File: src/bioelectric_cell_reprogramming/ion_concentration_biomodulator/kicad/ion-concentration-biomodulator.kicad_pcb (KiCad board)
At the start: 4 copper layers, 87.5 x 87.5 mm, 53 parts, among them J1 532610671, J10 39-53-2045, J11 Conn_01x14_Pin, J12 Conn_01x14_Pin, J13 39-53-2045, J14 39-53-2045, J15 Conn_ARM_SWD_TagConnect_TC2030, J16 IPL1-104-01-L-D-K, J17 Conn_01x02_Pin, J18 EJ508A, J19 USB_C_Receptacle_USB2.0_14P, J2 532610671, J3 532610671, J4 532610671, J5 S4B-PH-SM4-TB, J6 Conn_01x02_Pin, J7 6620XX11122_66200211122, J8 39-53-2045, J9 IPL1-102-01-L-S-K, Q1 NDT3055L, Q2 NDT3055L, Q3 NDT3055L, Q4 NDT3055L, Q5 NDT3055L, Q6 NDT3055L, SW1 SW_Push, U1 STM32F410CBTx, U2 LM1084-5.0, U3 LM1084-3.3, U4 USBLC6-2SC6

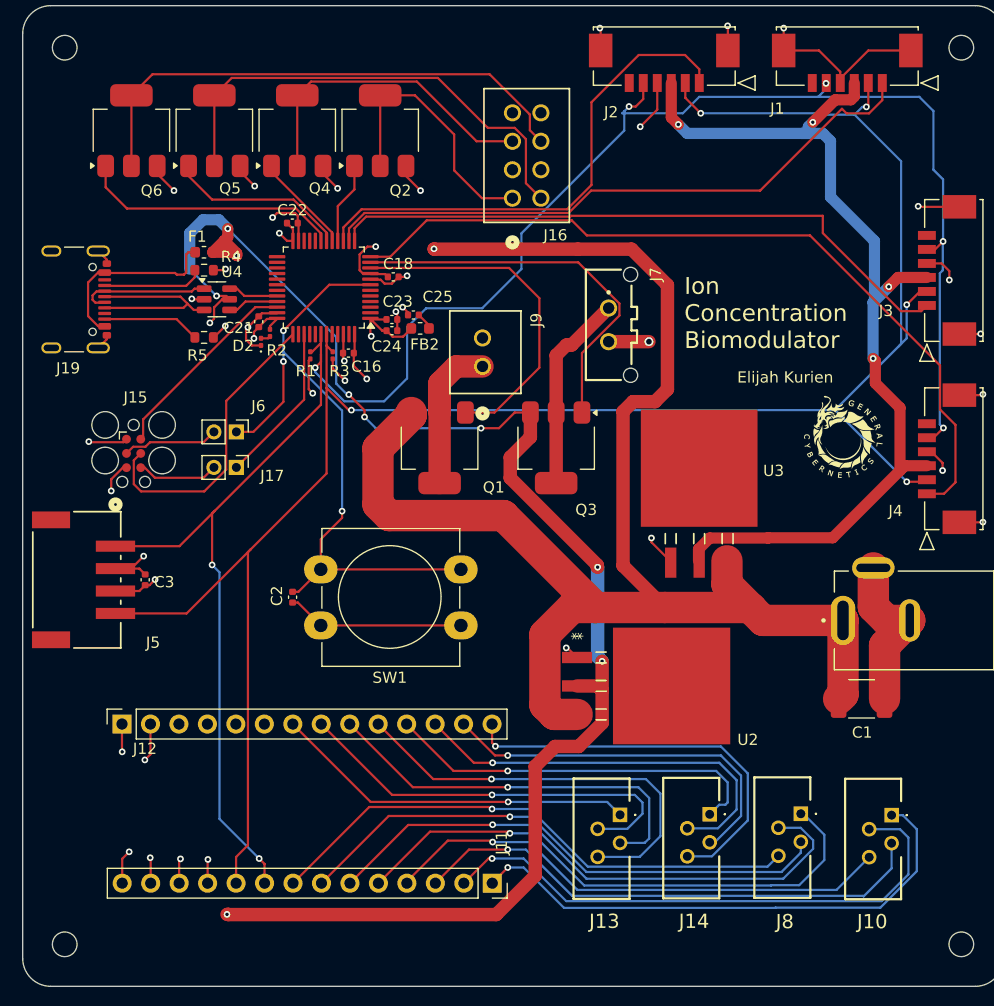
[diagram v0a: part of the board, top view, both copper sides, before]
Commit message: fix: replaced the USB connector with one in the JLCPCB parts library
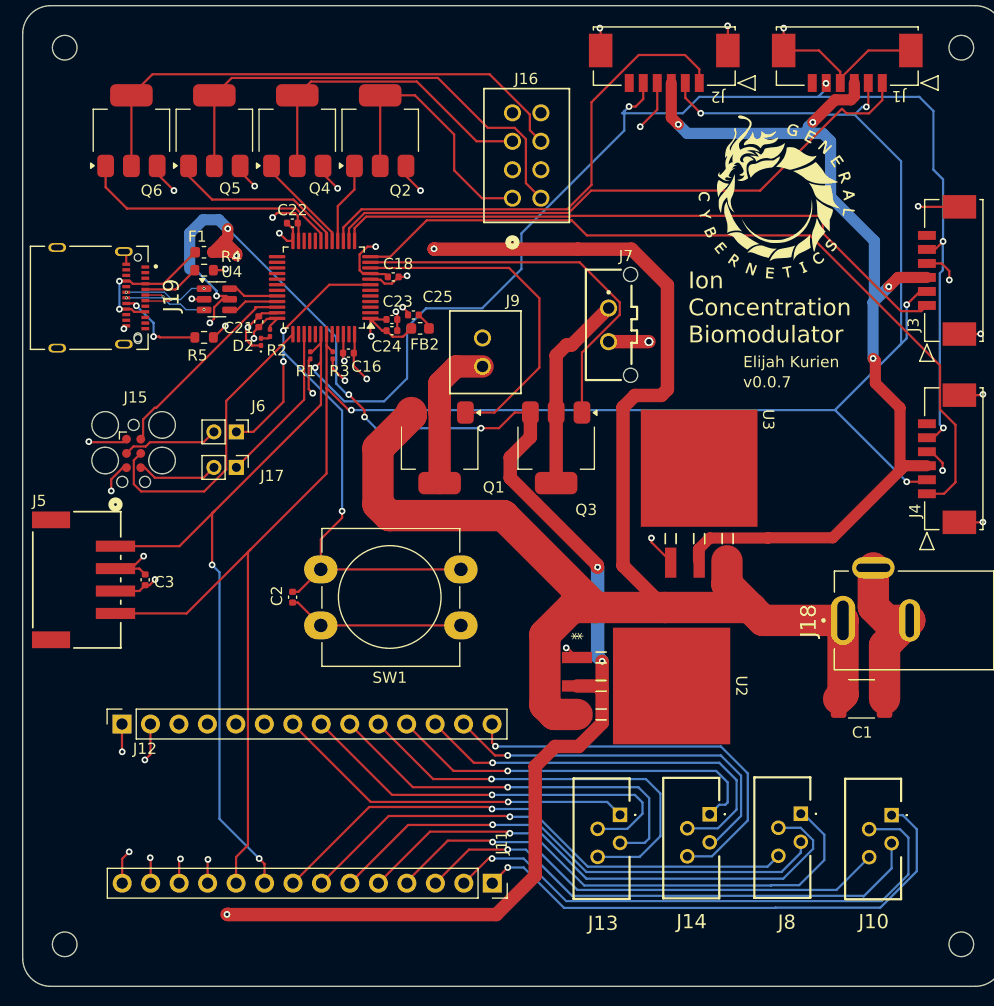
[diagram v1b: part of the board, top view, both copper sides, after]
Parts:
- J1, J2, J3, J4: footprint co2_sensor_footprint:CON_532610671 -> keyed_6_pin_horizontal_0532610671.pretty:CON_532610671
- J10, J13, J14, J8: footprint microfluidics:39532045 -> upright_4_pin_socket_39-53-2045.pretty:39532045
- J16: footprint pinch_solenoid:CONN_IPL1-104-01-x-D-x_SAI -> 2x04_socket_IPL1-104-01-L-D-K.pretty:CONN_IPL1-104-01-x-D-x_SAI
- J18: footprint barrel_jack_EJ508A:MPD_EJ508A -> Barrel_Jack_EJ508A.pretty:MPD_EJ508A
- J19: footprint Connector_USB:USB_C_Receptacle_GCT_USB4105-xx-A_16P_TopMnt_Horizontal -> 12401610E4_2A.pretty:AMPHENOL_12401610E4_2A
- J5: footprint co2_dev_board_male_socket:CONN4_S4B-PH-SM4-TB_JST -> male_socket_S4B-PH-SM4-TB.pretty:CONN4_S4B-PH-SM4-TB_JST
- J7: footprint peltier_cooler_socket_footprint:66200211122 -> 1x02_socket_66200211122.pretty:66200211122
- J9: footprint solenoid_footprint:CONN_IPL1-102-01-L-S-K_SAI -> 1x02_socket_IPL1-102-01-L-S-K.pretty:CONN_IPL1-102-01-L-S-K_SAI
- U2, U3: footprint LDO_5V:TS3B -> LDO_5V_LM1084.pretty:TS3B
- moved G*** 22.5 mm to (167.8, 66.3)
- moved J19 6.65 mm to (110.8, 75.3)
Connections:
- J19 pad A6: /D+ -> /D+_in
- J19 pad A7: /D- -> /D-_in
- J19 pad B6: /D+ -> /D+_in
- J19 pad B7: /D- -> /D-_in
- U4 pad 1: /D- -> /D-_in
- U4 pad 3: /D+ -> /D+_in
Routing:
- net /D+: track 21.5 -> 4.55 mm
- net /D-: track 16.5 -> 4.51 mm
- net /D-_in: track 0.00 -> 10.1 mm, vias 0 -> 3
- net /D+_in: track 0.00 -> 9.18 mm, vias 0 -> 3
- net /CC1: track 8.79 -> 5.14 mm
- net /VBUS: track 16.8 -> 13.4 mm, vias 0 -> 2
- net GND: track 120.6 -> 119.3 mm, vias 26 -> 27
- net /CC2: track 8.73 -> 8.09 mm, vias 0 -> 2
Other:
- board text added: "v0.0.7"

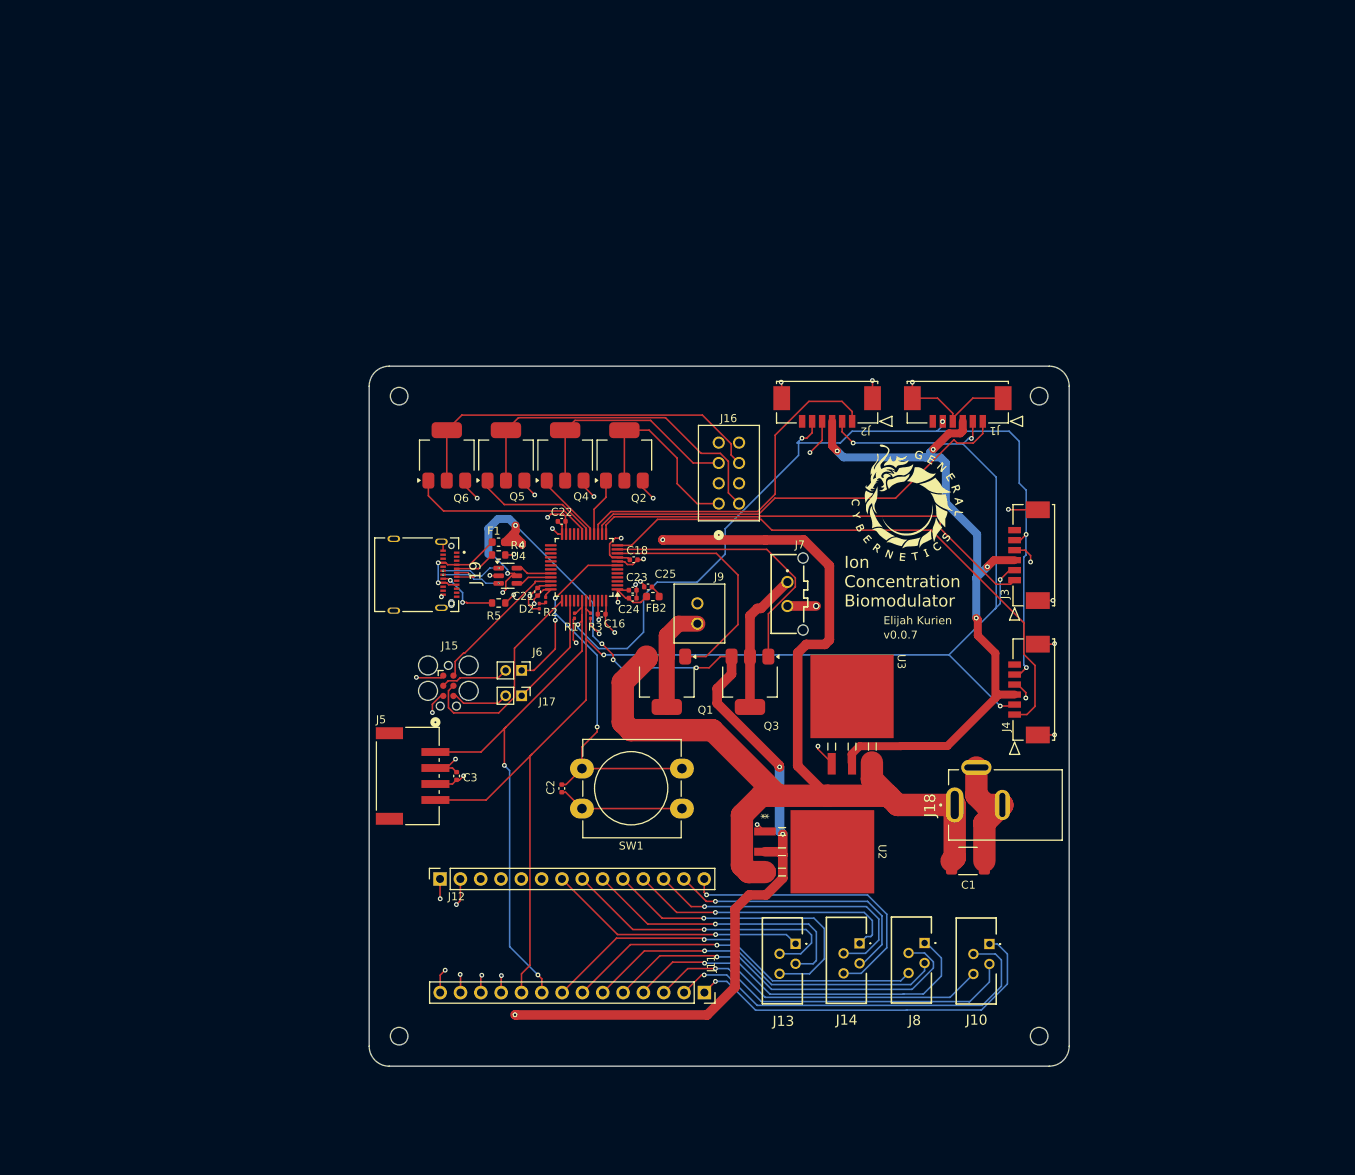
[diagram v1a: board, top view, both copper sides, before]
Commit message: fix: symbol and footprint libs, and improved routing
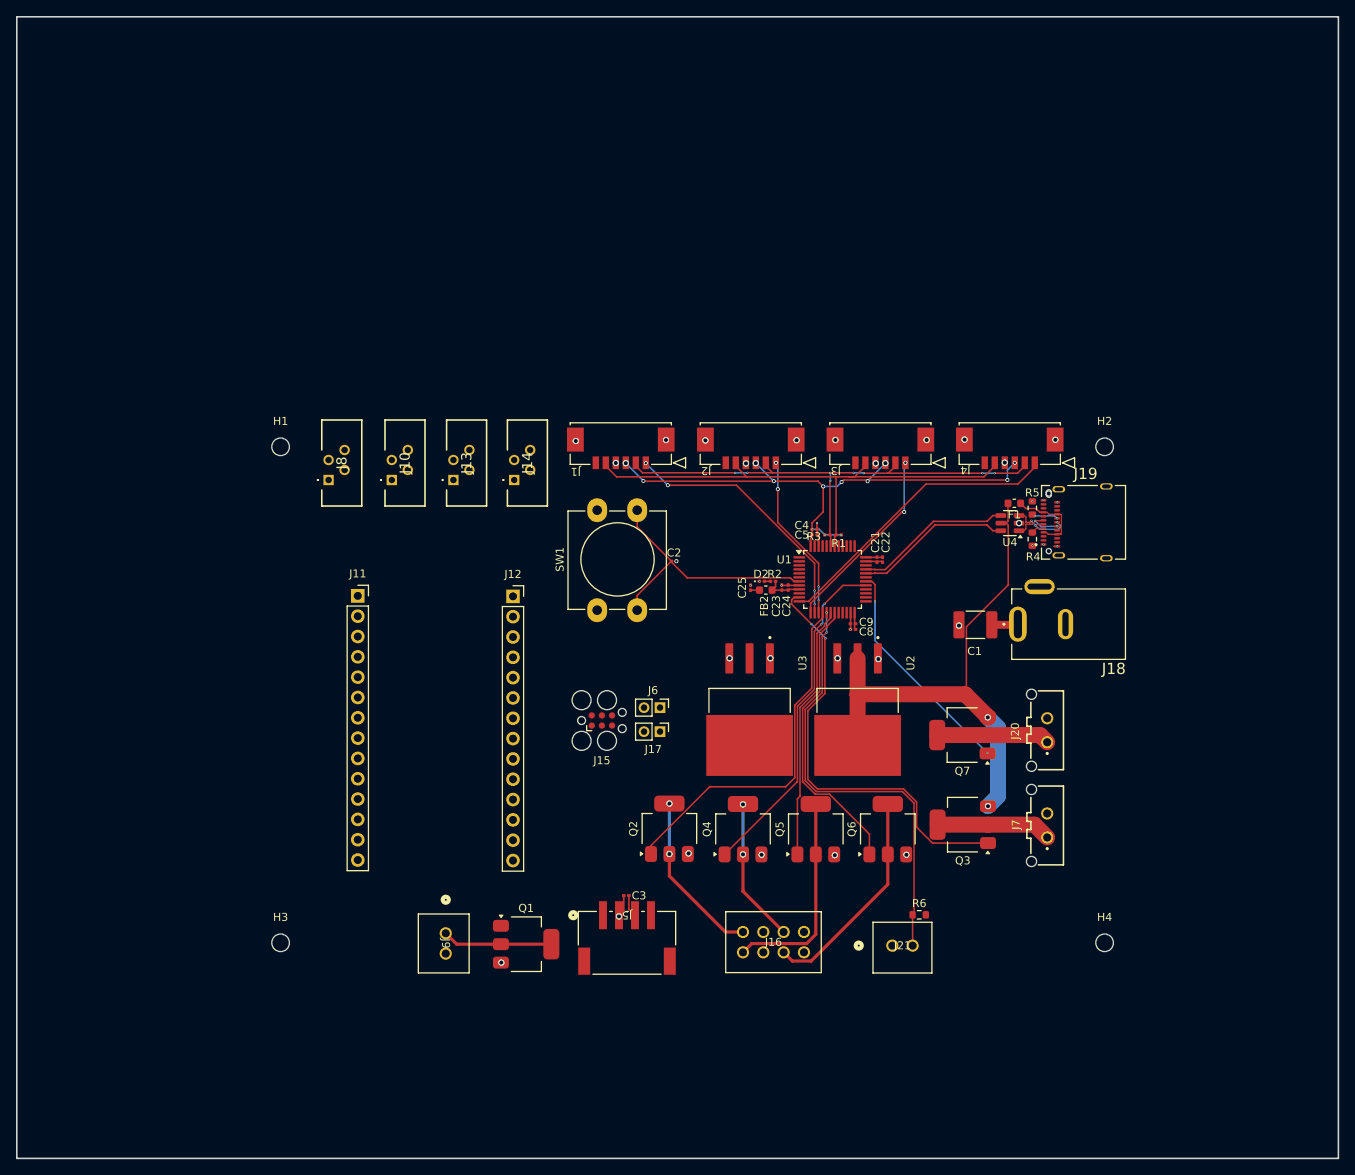
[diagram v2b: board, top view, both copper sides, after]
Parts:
- removed C16: 1uF, Capacitor_SMD:C_0402_1005Metric
- removed C18: 100nF, Capacitor_SMD:C_0402_1005Metric
- removed G***: LOGO, LOGO
- added C4: 100nF, Capacitor_SMD:C_0201_0603Metric, F.Cu at (156.2, 69.7)
- added C5: 1uF, Capacitor_SMD:C_0201_0603Metric, F.Cu at (156.2, 70.4)
- added C8: 100nF, Capacitor_SMD:C_0201_0603Metric, F.Cu at (160.9, 82.2)
- added C9: 1uF, Capacitor_SMD:C_0201_0603Metric, F.Cu at (160.9, 81.5)
- added J20: 6620XX11122_66200211122, 1x02_socket_66200211122.pretty:66200211122, F.Cu at (185.2, 94.8)
- added J21: IPL1-102-01-L-S-K, 1x02_socket_IPL1-102-01-L-S-K.pretty:CONN_IPL1-102-01-L-S-K_SAI, F.Cu at (165.9, 121.7)
- added Q7: NDT3055L, Package_TO_SOT_SMD:SOT-223-3_TabPin2, F.Cu at (174.6, 95.4)
- added R6: 10K, Resistor_SMD:R_0603_1608Metric, F.Cu at (169.2, 117.9)
- C2, C22, C23, C24, C25, C3: footprint Capacitor_SMD:C_0402_1005Metric -> Capacitor_SMD:C_0201_0603Metric
- C21: value 100nF -> 1uF; footprint Capacitor_SMD:C_0402_1005Metric -> Capacitor_SMD:C_0201_0603Metric
- R1, R3: value 10,000R -> 10K
- R2: value 220R -> 220
- R4, R5: value 5,100R -> 5K1
- U2: footprint LDO_5V_LM1084.pretty:TS3B -> LDO_5V_LM1084.pretty:TO254P1524X483-4N
- U3: footprint LDO_5V_LM1084.pretty:TS3B -> LDO_3V_LM1084.pretty:TO254P1524X483-4N
- moved H3 95.5 mm to (89.4, 121.3)
- moved J10 94.6 mm to (103.3, 63.5), turned to 90 degrees
- moved J8 94.3 mm to (95.4, 63.5), turned to 90 degrees
- moved H2 88.4 mm to (192.4, 59.4)
- moved H1 75.1 mm to (89.4, 59.4)
- moved J19 75.0 mm to (185.4, 68.8), turned to 90 degrees
- moved Q6 72.3 mm to (165.3, 107.1)
- moved J14 72.2 mm to (118.6, 63.5), turned to 90 degrees
- moved J13 72.0 mm to (111.0, 63.5), turned to 90 degrees
- moved H4 68.8 mm to (192.4, 121.3)
- moved R5 67.8 mm to (183.4, 67.0), turned to 90 degrees
- moved R4 66.7 mm to (183.4, 70.9), turned to -90 degrees
- moved J11 65.8 mm to (99.0, 78.0), turned to 0 degrees
- moved F1 64.7 mm to (181.1, 66.4), turned to 180 degrees
- moved U4 63.1 mm to (180.6, 68.9), turned to 180 degrees
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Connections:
- net Net-(J12-Pin_7) renamed /22-
- net Net-(J12-Pin_8) renamed /22+
- J19 pad A1: (no net) -> GND
- J19 pad A10: (no net) -> unconnected-(J19-RX2--PadA10)
- J19 pad A11: (no net) -> unconnected-(J19-RX2+-PadA11)
- J19 pad A12: (no net) -> GND
- J19 pad A2: (no net) -> unconnected-(J19-TX1+-PadA2)
- J19 pad A3: (no net) -> unconnected-(J19-TX1--PadA3)
- J19 pad A8: (no net) -> unconnected-(J19-SBU1-PadA8)
- J19 pad B10: (no net) -> unconnected-(J19-RX1--PadB10)
- J19 pad B11: (no net) -> unconnected-(J19-RX1+-PadB11)
- J19 pad B2: (no net) -> unconnected-(J19-TX2+-PadB2)
- J19 pad B3: (no net) -> unconnected-(J19-TX2--PadB3)
- J19 pad B8: (no net) -> unconnected-(J19-SBU2-PadB8)
- J19 pad S2: (no net) -> GND
- J19 pad S3: (no net) -> GND
- J19 pad S4: (no net) -> GND
- U1 pad 17: /SOL2 -> /THERM_FEEDBACK
- U1 pad 29: unconnected-(U1-PA8-Pad29) -> /SOL2
- U1 pad 30: unconnected-(U1-PA9-Pad30) -> /FRIDGE_PELT_OUT
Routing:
- net +12V: track 148.6 -> 3.30 mm, vias 5 -> 7
- net /I2C_SDA: track 182.0 -> 62.7 mm, vias 5 -> 8
- net /I2C_SCK: track 179.0 -> 64.6 mm, vias 7 -> 0
- net GND: track 119.3 -> 13.2 mm, vias 27 -> 29
- net +5V: track 150.0 -> 67.7 mm, vias 14 -> 2
- net /THERM_FEEDBACK: track 0.00 -> 54.7 mm, vias 0 -> 2
- net /32+: track 50.9 -> 0.00 mm, vias 1 -> 0
- net /42+: track 50.2 -> 0.00 mm, vias 1 -> 0
- net /32-: track 49.7 -> 0.00 mm, vias 1 -> 0
- net /31+: track 49.0 -> 0.00 mm, vias 1 -> 0
- net /31-: track 48.7 -> 0.00 mm, vias 1 -> 0
- net /42-: track 47.8 -> 0.00 mm, vias 1 -> 0
- net /41+: track 47.0 -> 0.00 mm, vias 1 -> 0
- net /41-: track 45.9 -> 0.00 mm, vias 1 -> 0
- net +3.3V: track 126.9 -> 82.4 mm
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- removed copper zone on In2.Cu, net +3.3V
- removed copper zone on In2.Cu, net +5V
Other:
- board size 87.5 x 87.5 mm -> 165.2 x 142.7 mm
- board text removed: "Elijah Kurien"
- board text removed: "Ion Concentration Biomodulator"
- board text removed: "v0.0.7"

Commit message: refactor: re-routed icbm
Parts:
- added G***: LOGO, LOGO, F.Cu at (133.0, 94.4)
- moved J9 65.1 mm to (175.2, 120.2)
- moved Q1 63.5 mm to (183.6, 121.5)
- moved J10 56.6 mm to (121.3, 117.1), turned to -90 degrees
- moved J8 56.3 mm to (112.5, 117.2), turned to -90 degrees
- moved J17 45.9 mm to (178.6, 73.0)
- moved J6 45.9 mm to (178.6, 76.0)
- moved J15 41.7 mm to (168.8, 79.3)
- moved J12 28.3 mm to (122.5, 106.1), turned to 180 degrees
- moved H1 14.0 mm to (103.4, 58.4)
- moved H3 14.0 mm to (103.4, 122.3)
- moved J11 9.64 mm to (107.6, 73.6)
- moved C2 5.01 mm to (141.9, 77.4)
- moved SW1 5.01 mm to (132.3, 83.5)
- moved J13 2.03 mm to (109.0, 63.5)
- moved H2 1.41 mm to (191.4, 58.4)
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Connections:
- U2 pad 4: (no net) -> +5V
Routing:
- net +3.3V: track 82.4 -> 205.9 mm, vias 13 -> 21
- net /I2C_SDA: track 62.7 -> 146.5 mm, vias 8 -> 11
- net /I2C_SCK: track 64.6 -> 139.9 mm, vias 0 -> 3
- net +5V: track 67.7 -> 138.9 mm, vias 2 -> 5
- net /SOLEN_OUT: track 0.00 -> 54.0 mm, vias 0 -> 2
- net /41+: track 0.00 -> 49.7 mm
- net /42-: track 0.00 -> 49.3 mm
- net /42+: track 0.00 -> 49.2 mm
- net /41-: track 0.00 -> 47.6 mm
- net /31+: track 0.00 -> 38.1 mm
- net /32+: track 0.00 -> 37.9 mm
- net /32-: track 0.00 -> 36.8 mm
- net /31-: track 0.00 -> 36.0 mm
- net /22-: track 0.00 -> 32.9 mm
- net /21+: track 0.00 -> 32.7 mm
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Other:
- board size 165.2 x 142.7 mm -> 96 x 72 mm
- board text added: "BOARD A"
- board text added: "Elijah Kurien Aydin Gokce"
- board text added: "Ion Concentration Biomodulator"

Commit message: mfg file for 0.0.8
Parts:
- moved J9 5.05 mm to (170.3, 121.6), turned to 0 degrees
- moved J21 4.83 mm to (161.0, 121.6)
- moved R6 4.83 mm to (164.4, 117.7)
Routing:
- net /CO2 Solenoid: track 12.1 -> 17.3 mm
- net +3.3V: track 205.9 -> 201.0 mm
- net /THERM_FEEDBACK: track 54.7 -> 56.6 mm
- net GND: track 20.7 -> 22.2 mm, vias 31 -> 32
